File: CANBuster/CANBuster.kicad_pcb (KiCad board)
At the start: 2 copper layers, 100 x 100 mm, 183 parts, among them CON1 BARREL_JACK, J1 RJ45, J2 RJ45, J3 RJ12, P1 CONN_01X10, P10 CONN_02X04, P11 RS232-Programmer, P12 S88, P13 CONN_01X10, P14 CONN_01X10, P15 TRACK, P16 CONN_01X02, P17 USB_B, P18 CONN_01X03, P2 CONN_01X10, P3 CONN_01X03, P4 CONN_01X03, P5 CONN_01X03, P6 CONN_01X03, P7 CONN_01X02, P8 CONN_01X06, P9 CONN_01X04, Q1 BC547, Q2 BC547, SW1 SW_PUSH, SW2 SW_PUSH, U1 PIC18F45K80, U12 MCP2561, U2 MCP2561, U3 7805, U4 LTV-844, U5 LTV-844, U6 LTV-844, U7 LTV-844, U8 ISO1050, Y1 16MHz

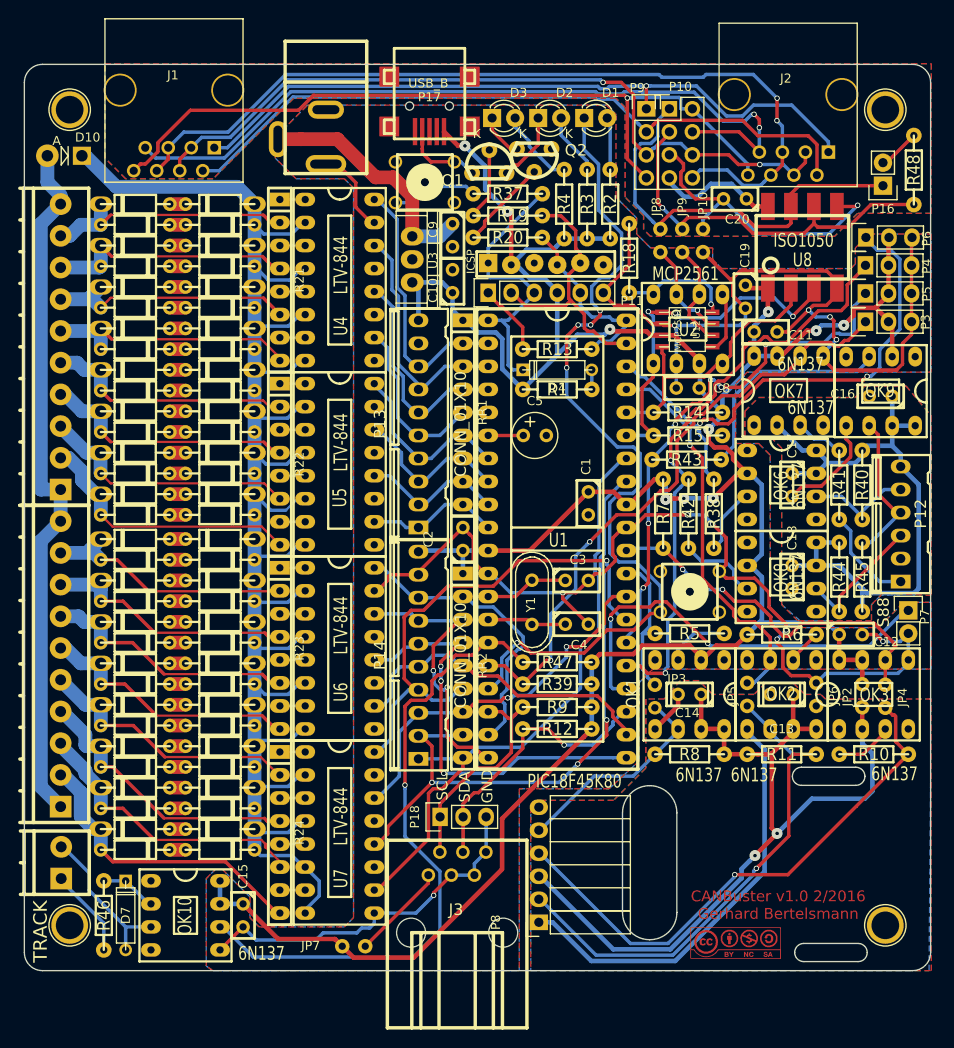
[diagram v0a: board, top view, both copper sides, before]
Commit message: fix USB power supply
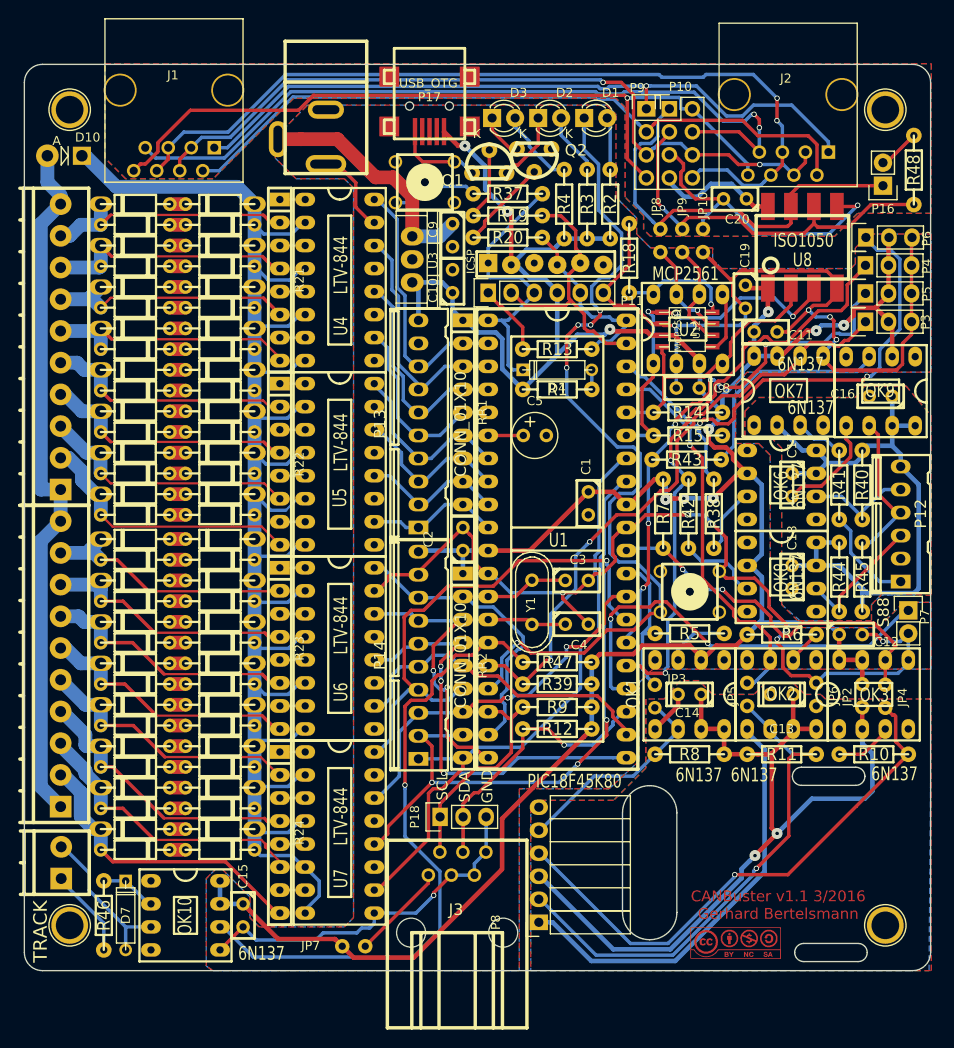
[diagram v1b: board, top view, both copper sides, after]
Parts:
- P17: value USB_B -> USB_OTG
- R11, R8: value 1K -> 390
- R38: value 330 -> 390
- R41: value 220 -> 390
- R47: value 1k5 -> 390
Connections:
- P17 pad 4: GND -> Net-(P17-Pad4)
- P17 pad 5: Net-(P17-Pad5) -> GND
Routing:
- net GND: track 258.6 -> 259.5 mm
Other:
- board text added: "CANBuster v1.1 3/2016 Gerhard Bertelsmann"
- board text removed: "CANBuster v1.0 2/2016 Gerhard Bertelsmann"

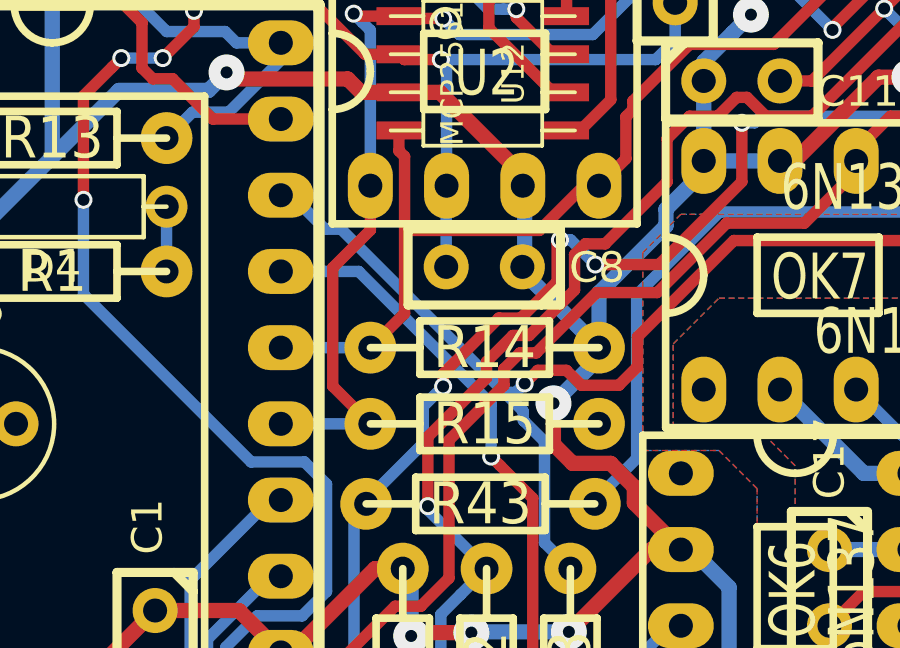
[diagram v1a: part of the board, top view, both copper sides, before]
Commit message: remove unused R14 and R15
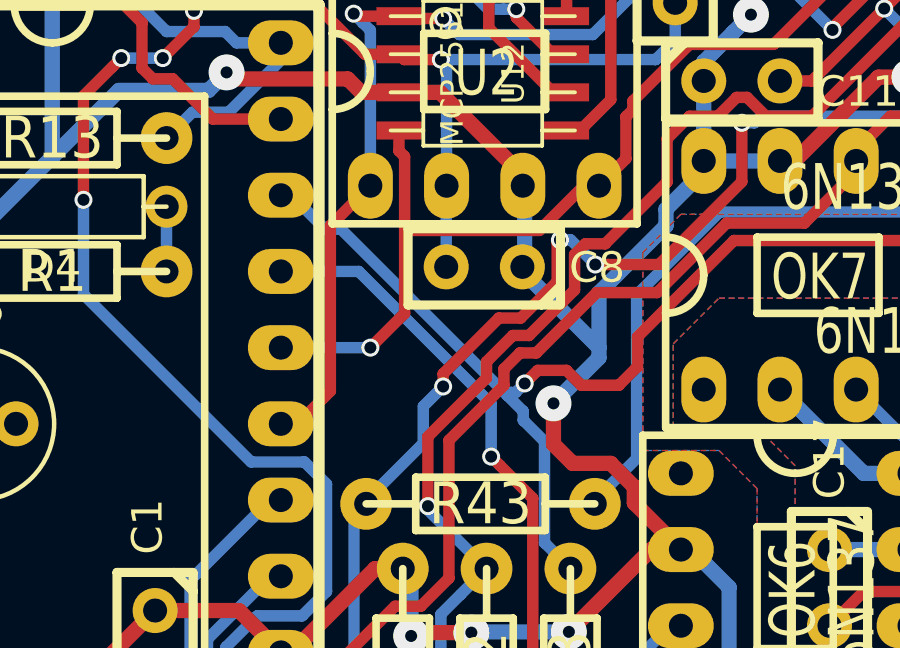
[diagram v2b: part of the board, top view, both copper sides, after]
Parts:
- removed R14: 1k5, w_pth_resistors:RC03
- removed R15: 390, w_pth_resistors:RC03
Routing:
- net /CANTX: track 40.0 -> 37.6 mm
- net /CANRX: vias 0 -> 1

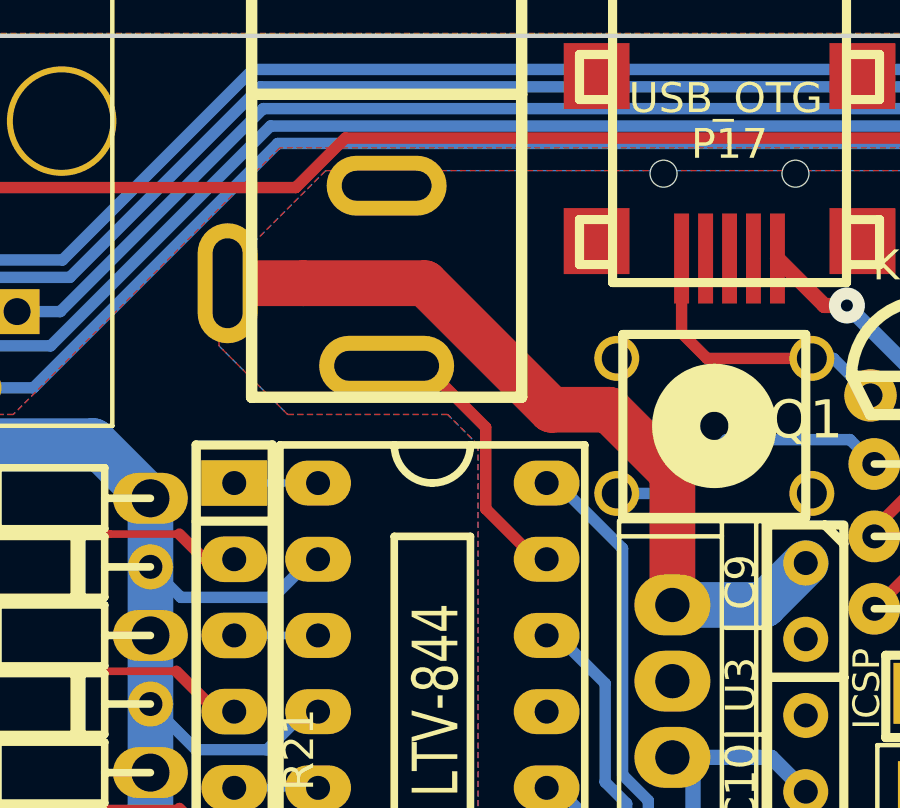
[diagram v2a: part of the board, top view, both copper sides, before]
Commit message: fix power jack
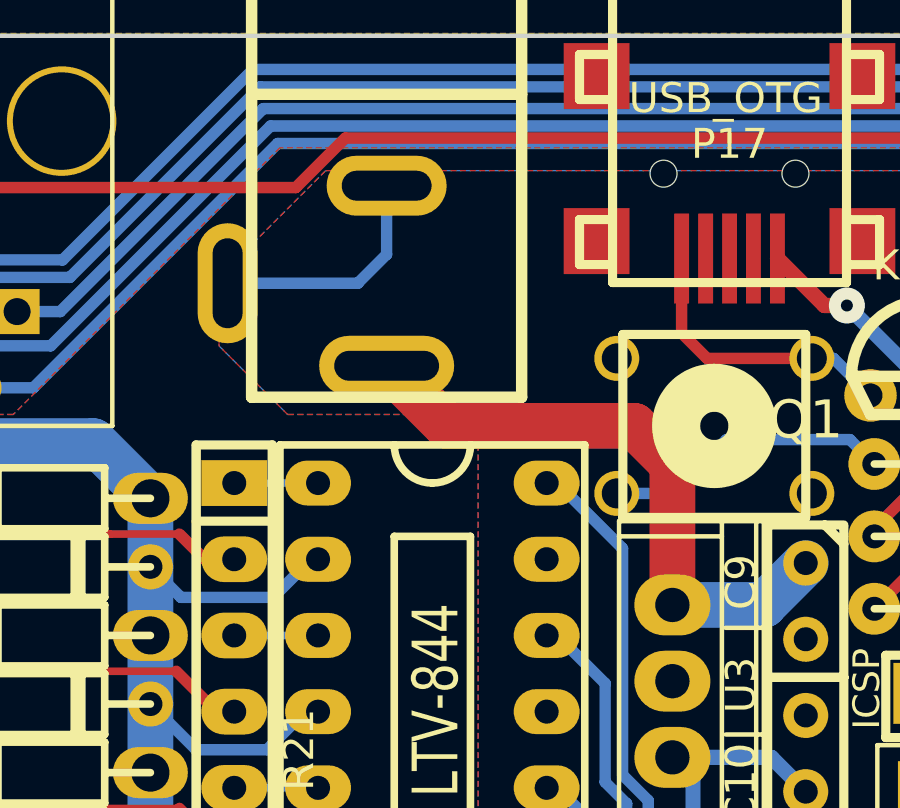
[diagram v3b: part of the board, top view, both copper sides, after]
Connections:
- CON1 pad 1: Net-(C9-Pad1) -> GND
- CON1 pad 3: GND -> Net-(C9-Pad1)
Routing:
- net Net-(C9-Pad1): track 26.9 -> 21.9 mm
- net GND: track 259.5 -> 258.2 mm
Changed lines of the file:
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@@
-(kicad_pcb (version 4) (host pcbnew 4.0.2-4+6225~38~ubuntu14.04.1-stable)
+(kicad_pcb (version 4) (host pcbnew 4.0.1-stable)
   (general
     (links 461)
     (no_connects 0)
-    (area 70.028999 35.052999 170.179001 135.203001)
+    (area 69.215499 29.4545 181.99 144.85554)
     (thickness 1.6)
     (drawings 32)
-    (tracks 1735)
+    (tracks 1733)
     (zones 0)
     (modules 181)
@@
     (fp_line (start -4.50088 -7.29996) (end -4.50088 7.29996) (layer F.SilkS) (width 0.381))
     (pad 1 thru_hole oval (at 5.30098 -3.50012 180) (size 1.99898 4.0005) (drill oval 1.00076 2.99974) (layers *.Cu *.Mask F.SilkS)
-      (net 58 "Net-(C9-Pad1)"))
+      (net 2 GND))
     (pad 2 thru_hole oval (at 0 -0.24892 180) (size 4.0005 1.99898) (drill oval 2.99974 1.00076) (layers *.Cu *.Mask F.SilkS)
       (net 2 GND))
     (pad 3 thru_hole oval (at 0 -6.25094 180) (size 4.50088 1.99898) (drill oval 3.50012 1.00076) (layers *.Cu *.Mask F.SilkS)
-      (net 2 GND))
+      (net 58 "Net-(C9-Pad1)"))
     (model walter/conn_misc/dc_socket.wrl
       (at (xyz 0 0 0))
@@
   (segment (start 91.694 125.222) (end 91.694 127.762) (width 0.508) (layer B.Cu) (net 1))
   (segment (start 91.694 127.762) (end 94.234 127.762) (width 0.508) (layer B.Cu) (net 1))
+  (segment (start 98.07702 43.37812) (end 102.41788 43.37812) (width 0.381) (layer B.Cu) (net 2))
+  (segment (start 103.378 42.418) (end 103.378 40.12692) (width 0.381) (layer B.Cu) (net 2))
+  (segment (start 102.41788 43.37812) (end 103.378 42.418) (width 0.381) (layer B.Cu) (net 2))
   (segment (start 117.5512 45.88256) (end 114.05616 45.88256) (width 0.381) (layer F.Cu) (net 2))
   (segment (start 113.21034 45.03674) (end 113.21034 42.554) (width 0.381) (layer F.Cu) (net 2))
   (segment (start 114.05616 45.88256) (end 113.21034 45.03674) (width 0.381) (layer F.Cu) (net 2))
   (segment (start 108.712 52.578) (end 108.36275 52.578) (width 0.381) (layer F.Cu) (net 2))
-  (segment (start 108.36275 52.578) (end 106.68 50.89525) (width 0.381) (layer F.Cu) (net 2))
-  (segment (start 106.68 50.89525) (end 106.68 48.17999) (width 0.381) (layer F.Cu) (net 2))
-  (segment (start 106.68 48.17999) (end 104.62895 46.12894) (width 0.381) (layer F.Cu) (net 2))
-  (segment (start 104.62895 46.12894) (end 103.378 46.12894) (width 0.381) (layer F.Cu) (net 2))
   (segment (start 146.05 85.852) (end 147.536599 87.338599) (width 0.381) (layer F.Cu) (net 2))
   (segment (start 147.536599 87.338599) (end 147.536599 90.319161) (width 0.381) (layer F.Cu) (net 2))
@@
   (segment (start 146.05 61.7728) (end 145.8722 61.595) (width 0.381) (layer F.Cu) (net 57))
   (via (at 145.8722 61.595) (size 0.6) (drill 0.4) (layers F.Cu B.Cu) (net 57))
+  (segment (start 112.903 54.102) (end 112.903 49.403) (width 1.524) (layer F.Cu) (net 58))
+  (segment (start 105.38206 48.133) (end 103.378 46.12894) (width 1.524) (layer F.Cu) (net 58))
+  (segment (start 111.633 48.133) (end 105.38206 48.133) (width 1.524) (layer F.Cu) (net 58))
+  (segment (start 112.903 49.403) (end 111.633 48.133) (width 1.524) (layer F.Cu) (net 58))
+  (segment (start 104.62895 46.12894) (end 103.378 46.12894) (width 0.381) (layer F.Cu) (net 58))
   (segment (start 112.903 54.102) (end 115.951 54.102) (width 1.524) (layer B.Cu) (net 58))
   (segment (start 115.951 54.102) (end 117.348 52.705) (width 1.524) (layer B.Cu) (net 58))
-  (segment (start 112.903 54.102) (end 112.903 49.703878) (width 1.524) (layer F.Cu) (net 58))
-  (segment (start 112.903 49.703878) (end 110.793683 47.594561) (width 1.524) (layer F.Cu) (net 58))
-  (segment (start 110.793683 47.594561) (end 108.86855 47.594561) (width 1.524) (layer F.Cu) (net 58))
-  (segment (start 108.86855 47.594561) (end 104.652109 43.37812) (width 1.524) (layer F.Cu) (net 58))
-  (segment (start 104.652109 43.37812) (end 100.60051 43.37812) (width 1.524) (layer F.Cu) (net 58))
-  (segment (start 100.60051 43.37812) (end 98.07702 43.37812) (width 1.524) (layer F.Cu) (net 58))
   (segment (start 132.588 63.881) (end 131.206978 63.881) (width 0.381) (layer B.Cu) (net 59))
   (via (at 131.206978 63.881) (size 0.6) (drill 0.4) (layers F.Cu B.Cu) (net 59))

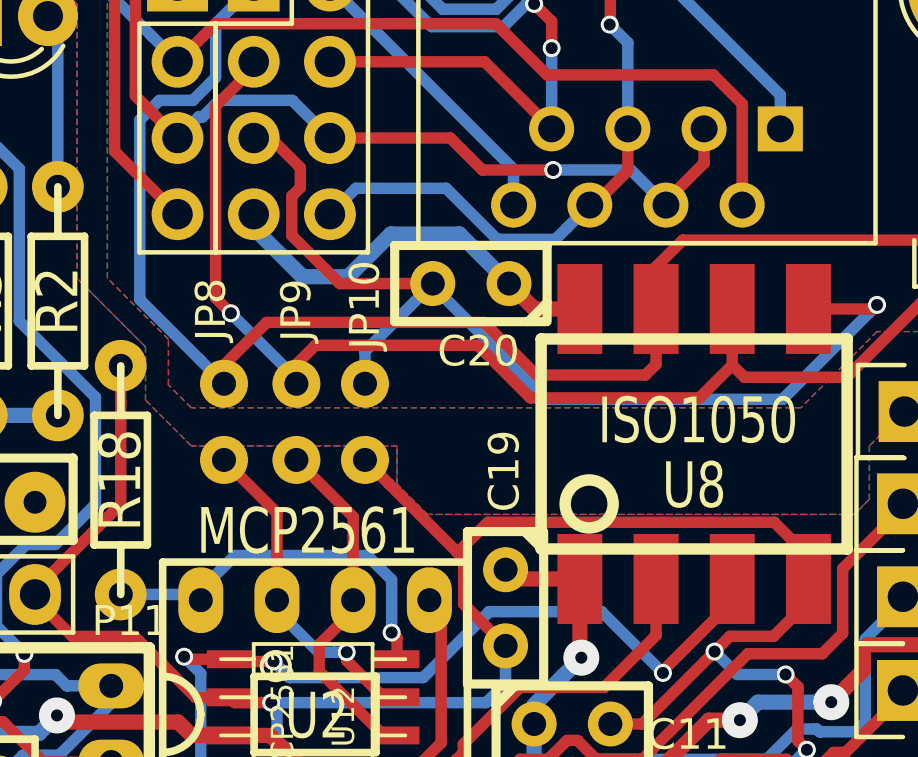
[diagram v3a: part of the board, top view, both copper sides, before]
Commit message: add %V jumper
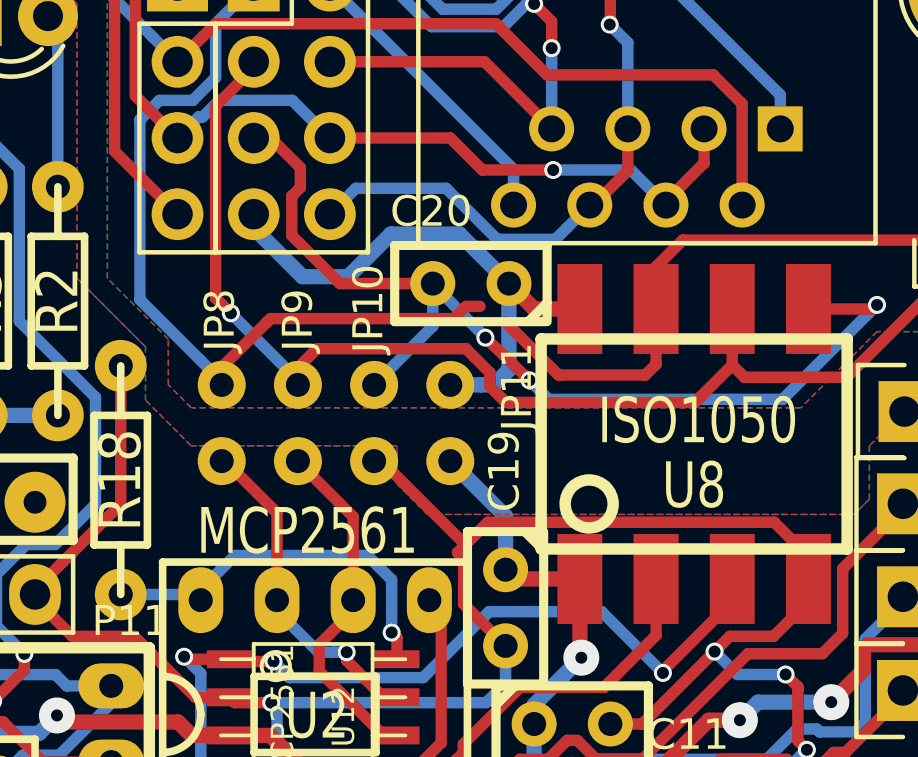
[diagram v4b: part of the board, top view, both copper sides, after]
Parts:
- added JP11: JUMPER, Wire_Pads:SolderWirePad_2x_0-2.54mmDrill, F.Cu at (147.8, 54.6)
- JP10, JP8, JP9: footprint jumper:SolderWirePad_2x_0-2.54mmDrill -> Wire_Pads:SolderWirePad_2x_0-2.54mmDrill
- moved JP10 0.31 mm to (145.3, 54.6)
- moved JP8 0.09 mm to (140.2, 54.6)
- moved JP9 0.06 mm to (142.7, 54.6)
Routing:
- net +5V: track 13.6 -> 18.7 mm
- net VDD: track 329.3 -> 333.7 mm
- net /CANH: track 46.9 -> 46.3 mm
- net GNDD: vias 1 -> 3
